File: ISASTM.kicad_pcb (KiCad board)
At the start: 2 copper layers, 1 part, among them J1 Bus_ISA_16bit

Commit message: Add connector
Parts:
- J1: value Bus_ISA_16bit -> Bus_ISA_8bit; footprint isastm:ISA16 -> ISASTM:Conn_Edge_PCB_ISA8
- moved J1 43.0 mm to (76.2, 112.4)
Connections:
- net Net-(J1-Pad11) renamed /~SMEMW
- net Net-(J1-Pad12) renamed /~SMEMR
- net Net-(J1-Pad13) renamed /~IOW
- net Net-(J1-Pad14) renamed /~IOR
- net Net-(J1-Pad15) renamed /~DACK3
- net Net-(J1-Pad16) renamed /DRQ3
- net Net-(J1-Pad17) renamed /~DACK1
- net Net-(J1-Pad18) renamed /DRQ1
- net Net-(J1-Pad19) renamed /~REFRESH
- net Net-(J1-Pad2) renamed /RESET
- net Net-(J1-Pad20) renamed /CLK
- net Net-(J1-Pad21) renamed /IRQ7
- net Net-(J1-Pad22) renamed /IRQ6
- net Net-(J1-Pad23) renamed /IRQ5
- net Net-(J1-Pad24) renamed /IRQ4
- net Net-(J1-Pad25) renamed /IRQ3
- net Net-(J1-Pad26) renamed /~DACK2
- net Net-(J1-Pad27) renamed /TC
- net Net-(J1-Pad28) renamed /ALE
- net Net-(J1-Pad30) renamed /OSC
- net Net-(J1-Pad32) renamed /~IO_CH_CK
- net Net-(J1-Pad33) renamed /D7
- net Net-(J1-Pad34) renamed /D6
- net Net-(J1-Pad35) renamed /D5
- net Net-(J1-Pad36) renamed /D4
- net Net-(J1-Pad37) renamed /D3
- net Net-(J1-Pad38) renamed /D2
- net Net-(J1-Pad39) renamed /D1
- net Net-(J1-Pad4) renamed /IRQ2
- net Net-(J1-Pad40) renamed /D0
- net Net-(J1-Pad41) renamed /IO_CH_RDY
- net Net-(J1-Pad42) renamed /AEN
- net Net-(J1-Pad43) renamed /A19
- net Net-(J1-Pad44) renamed /A18
- net Net-(J1-Pad45) renamed /A17
- net Net-(J1-Pad46) renamed /A16
- net Net-(J1-Pad47) renamed /A15
- net Net-(J1-Pad48) renamed /A14
- net Net-(J1-Pad49) renamed /A13
- net Net-(J1-Pad5) renamed -5V
- net Net-(J1-Pad50) renamed /A12
- net Net-(J1-Pad51) renamed /A11
- net Net-(J1-Pad52) renamed /A10
- net Net-(J1-Pad53) renamed /A9
- net Net-(J1-Pad54) renamed /A8
- net Net-(J1-Pad55) renamed /A7
- net Net-(J1-Pad56) renamed /A6
- net Net-(J1-Pad57) renamed /A5
- net Net-(J1-Pad58) renamed /A4
- net Net-(J1-Pad59) renamed /A3
- net Net-(J1-Pad6) renamed /DRQ2
- net Net-(J1-Pad60) renamed /A2
- net Net-(J1-Pad61) renamed /A1
- net Net-(J1-Pad62) renamed /A0
- net Net-(J1-Pad7) renamed -12V
- net Net-(J1-Pad9) renamed +12V
- J1 pad 29: Net-(J1-Pad29) -> +5V
- J1 pad 3: Net-(J1-Pad3) -> +5V
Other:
- board outline added: 101.6 x 101.6 mm
- copper layers 2 -> 4
- board text added: "Back ->"

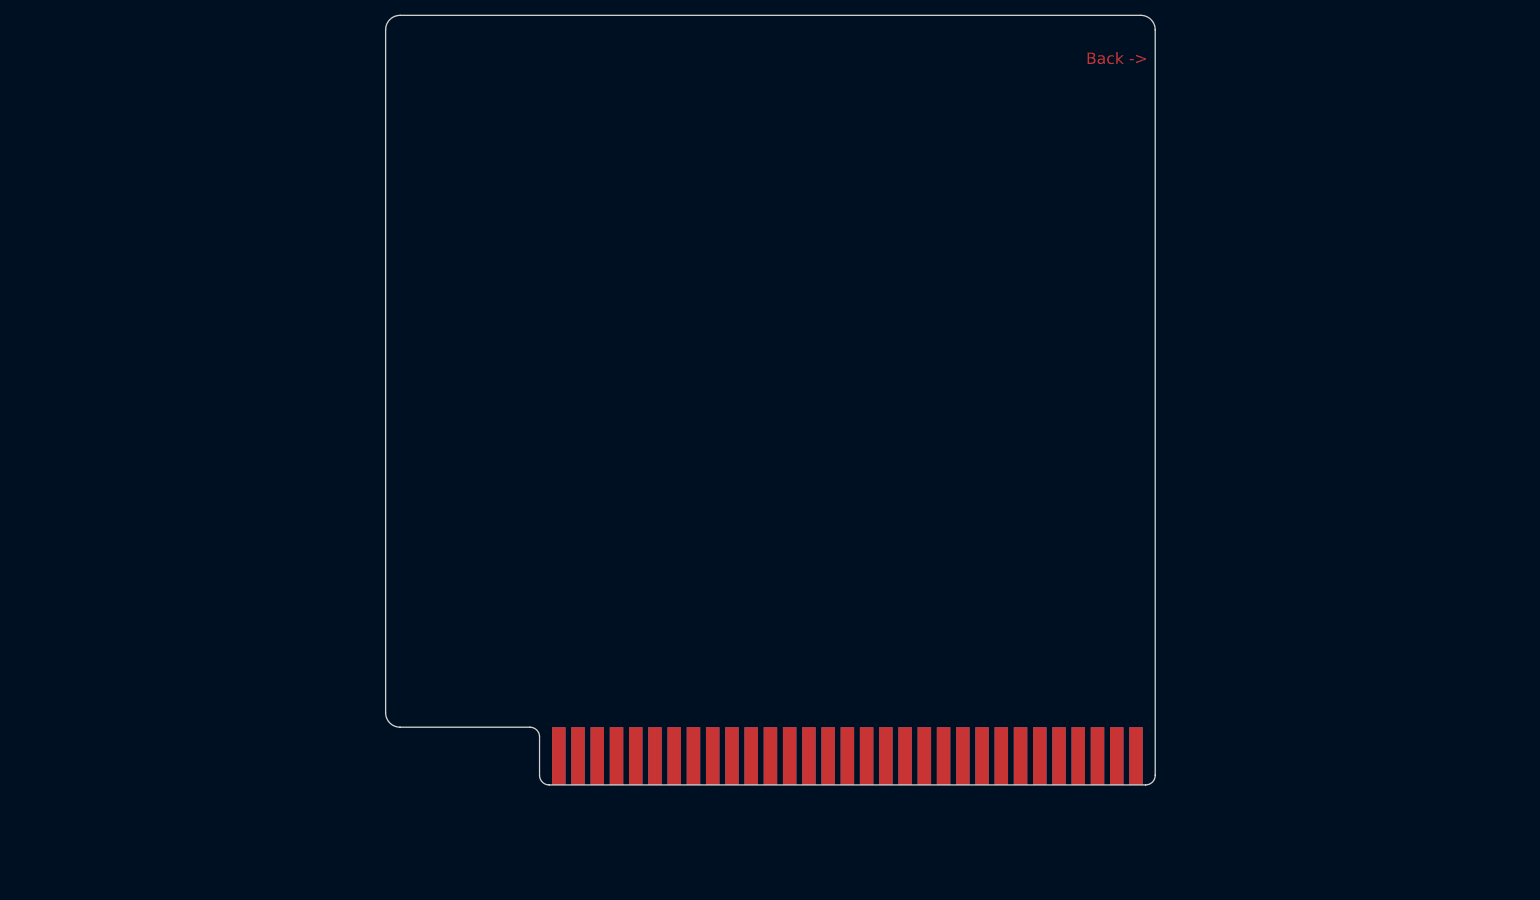
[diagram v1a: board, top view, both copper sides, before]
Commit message: Add ISA bus, level shifters, memory pinout
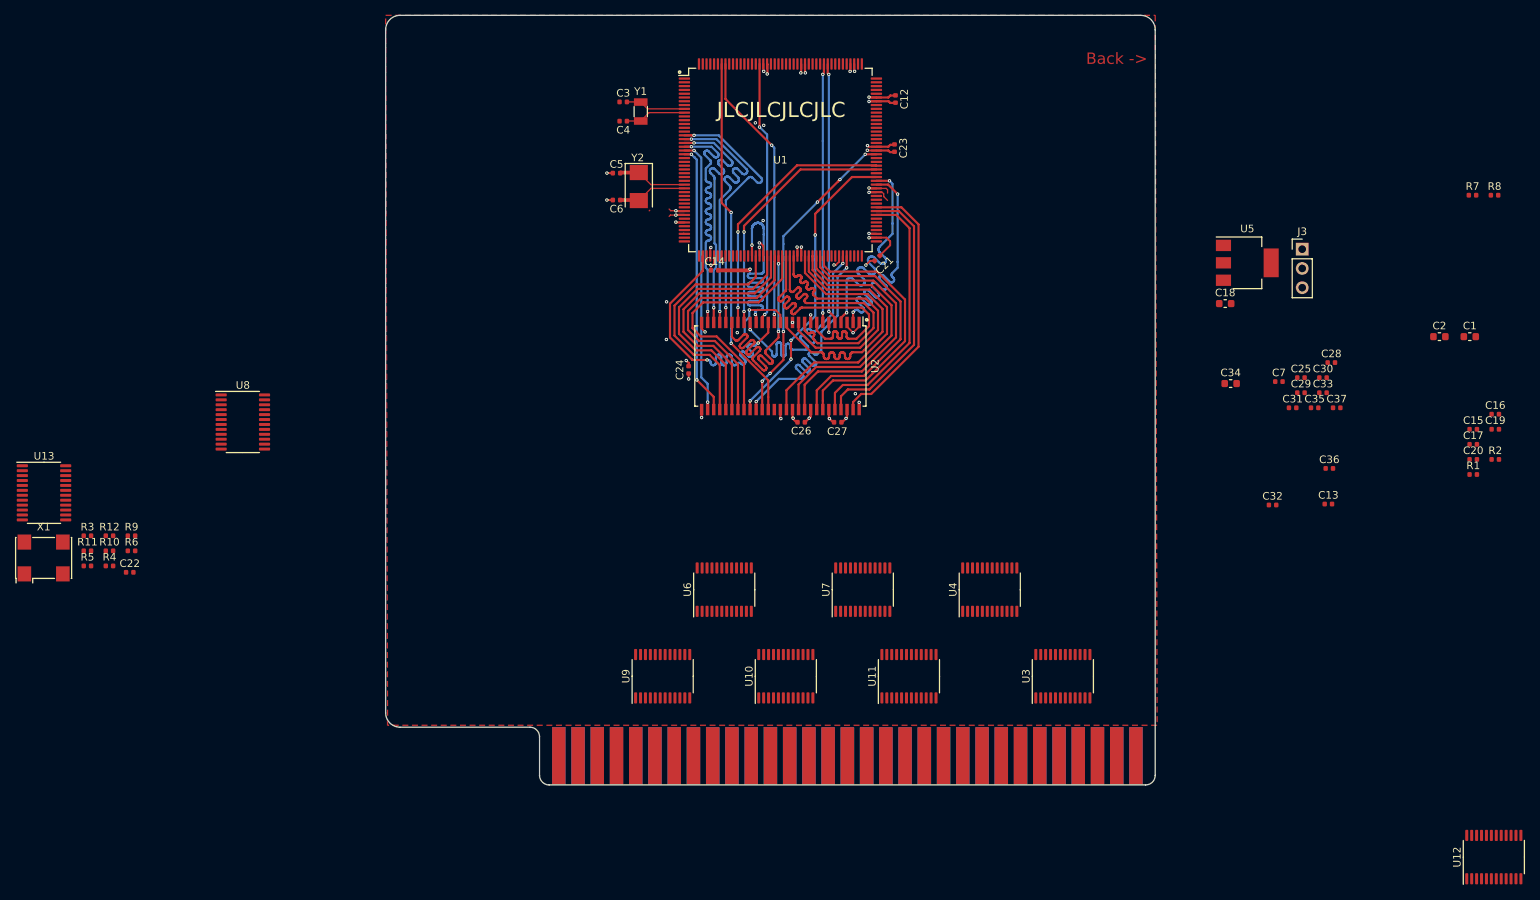
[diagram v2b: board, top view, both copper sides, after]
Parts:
- added C1: 2.2u, Capacitor_SMD:C_0603_1608Metric, F.Cu at (158.4, 57.0)
- added C12: 100n, Capacitor_SMD:C_0402_1005Metric, F.Cu at (82.5, 25.7)
- added C13: 100n, Capacitor_SMD:C_0402_1005Metric, F.Cu at (139.7, 79.1)
- added C14: 100n, Capacitor_SMD:C_0402_1005Metric, F.Cu at (58.7, 48.3)
- added C15: 100n, Capacitor_SMD:C_0402_1005Metric, F.Cu at (158.8, 69.3)
- added C16: 100n, Capacitor_SMD:C_0402_1005Metric, F.Cu at (161.7, 67.3)
- added C17: 100n, Capacitor_SMD:C_0402_1005Metric, F.Cu at (158.8, 71.2)
- added C18: 10u, Capacitor_SMD:C_0603_1608Metric, F.Cu at (126.1, 52.7)
- added C19: 100n, Capacitor_SMD:C_0402_1005Metric, F.Cu at (161.7, 69.3)
- added C2: 2.2u, Capacitor_SMD:C_0603_1608Metric, F.Cu at (154.4, 57.0)
- added C20: 100n, Capacitor_SMD:C_0402_1005Metric, F.Cu at (158.8, 73.2)
- added C21: 100n, Capacitor_SMD:C_0402_1005Metric, F.Cu at (80.1, 46.7)
- added C22: 100n, Capacitor_SMD:C_0402_1005Metric, F.Cu at (-18.5, 88.1)
- added C23: 100n, Capacitor_SMD:C_0402_1005Metric, F.Cu at (82.4, 32.1)
- added C24: 100n, Capacitor_SMD:C_0402_1005Metric, F.Cu at (55.2, 61.4)
- added C25: 100n, Capacitor_SMD:C_0402_1005Metric, F.Cu at (136.1, 62.4)
- added C26: 100n, Capacitor_SMD:C_0402_1005Metric, F.Cu at (70.1, 68.3)
- added C27: 100n, Capacitor_SMD:C_0402_1005Metric, F.Cu at (74.9, 68.3)
- added C28: 100n, Capacitor_SMD:C_0402_1005Metric, F.Cu at (140.1, 60.4)
- added C29: 100n, Capacitor_SMD:C_0402_1005Metric, F.Cu at (136.1, 64.4)
- added C3: 6p, Capacitor_SMD:C_0402_1005Metric, F.Cu at (46.6, 26.0)
- added C30: 100n, Capacitor_SMD:C_0402_1005Metric, F.Cu at (139.0, 62.4)
- added C31: 100n, Capacitor_SMD:C_0402_1005Metric, F.Cu at (135.0, 66.4)
- added C32: 100n, Capacitor_SMD:C_0402_1005Metric, F.Cu at (132.3, 79.2)
- added C33: 1u, Capacitor_SMD:C_0402_1005Metric, F.Cu at (139.0, 64.4)
- added C34: 22u, Capacitor_SMD:C_0603_1608Metric, F.Cu at (126.8, 63.2)
- added C35: 100n, Capacitor_SMD:C_0402_1005Metric, F.Cu at (137.9, 66.4)
- added C36: 100n, Capacitor_SMD:C_0402_1005Metric, F.Cu at (139.8, 74.4)
- added C37: 100n, Capacitor_SMD:C_0402_1005Metric, F.Cu at (140.8, 66.4)
- added C4: 6p, Capacitor_SMD:C_0402_1005Metric, F.Cu at (46.6, 28.6)
- added C5: 20p, Capacitor_SMD:C_0402_1005Metric, F.Cu at (45.7, 35.4)
- added C6: 20p, Capacitor_SMD:C_0402_1005Metric, F.Cu at (45.7, 39.0)
- added C7: 1u, Capacitor_SMD:C_0402_1005Metric, F.Cu at (133.2, 63.0)
- added J3: Boot select, Connector_PinHeader_2.54mm:PinHeader_1x03_P2.54mm_Vertical, F.Cu at (136.2, 45.5)
- added R1: 10k, Resistor_SMD:R_0402_1005Metric, F.Cu at (158.8, 75.2)
- added R10: 10k, Resistor_SMD:R_0402_1005Metric, F.Cu at (-21.2, 85.3)
- added R11: 10k, Resistor_SMD:R_0402_1005Metric, F.Cu at (-24.1, 85.3)
- added R12: 10k, Resistor_SMD:R_0402_1005Metric, F.Cu at (-21.2, 83.3)
- added R2: 10R, Resistor_SMD:R_0402_1005Metric, F.Cu at (161.7, 73.2)
- added R3: 10k, Resistor_SMD:R_0402_1005Metric, F.Cu at (-24.1, 83.3)
- added R4: 10k, Resistor_SMD:R_0402_1005Metric, F.Cu at (-21.2, 87.3)
- added R5: 10k, Resistor_SMD:R_0402_1005Metric, F.Cu at (-24.1, 87.3)
- added R6: 10k, Resistor_SMD:R_0402_1005Metric, F.Cu at (-18.3, 85.3)
- added R7: 10k, Resistor_SMD:R_0402_1005Metric, F.Cu at (158.7, 38.4)
- added R8: 100k, Resistor_SMD:R_0402_1005Metric, F.Cu at (161.6, 38.4)
- added R9: 10k, Resistor_SMD:R_0402_1005Metric, F.Cu at (-18.3, 83.3)
- added U1: STM32H743IITx, Package_QFP:LQFP-176_24x24mm_P0.5mm, F.Cu at (67.4, 33.7)
- added U10: SN74AVC8T245PW, Package_SO:TSSOP-24_4.4x7.8mm_P0.65mm, F.Cu at (68.1, 101.9)
- added U11: SN74AVC8T245PW, Package_SO:TSSOP-24_4.4x7.8mm_P0.65mm, F.Cu at (84.3, 101.9)
- added U12: SN74AVC8T245PW, Package_SO:TSSOP-24_4.4x7.8mm_P0.65mm, F.Cu at (161.5, 125.7)
- added U13: SN74AVC8T245PW, Package_SO:TSSOP-24_4.4x7.8mm_P0.65mm, F.Cu at (-29.9, 77.6)
- added U2: MT48LC16M16A2P, Package_SO:TSOP-II-54_22.2x10.16mm_P0.8mm, F.Cu at (67.4, 60.9)
- added U3: SN74AVC8T245PW, Package_SO:TSSOP-24_4.4x7.8mm_P0.65mm, F.Cu at (104.6, 101.9)
- added U4: SN74AVC8T245PW, Package_SO:TSSOP-24_4.4x7.8mm_P0.65mm, F.Cu at (95.0, 90.4)
- added U5: AMS1117-3.3, Package_TO_SOT_SMD:SOT-223-3_TabPin2, F.Cu at (129.0, 47.3)
- added U6: SN74AVC8T245PW, Package_SO:TSSOP-24_4.4x7.8mm_P0.65mm, F.Cu at (59.9, 90.4)
- added U7: SN74AVC8T245PW, Package_SO:TSSOP-24_4.4x7.8mm_P0.65mm, F.Cu at (78.2, 90.4)
- added U8: SN74AVC8T245PW, Package_SO:TSSOP-24_4.4x7.8mm_P0.65mm, F.Cu at (-3.61, 68.3)
- added U9: SN74AVC8T245PW, Package_SO:TSSOP-24_4.4x7.8mm_P0.65mm, F.Cu at (51.8, 101.9)
- added X1: SG-7050CAN, Oscillator:Oscillator_SMD_SeikoEpson_SG8002CA-4Pin_7.0x5.0mm, F.Cu at (-29.9, 86.2)
- added Y1: 32.768 kHz, Crystal:Crystal_SMD_3215-2Pin_3.2x1.5mm, F.Cu at (48.9, 27.3)
- added Y2: 8 MHz, Crystal:Crystal_SMD_5032-2Pin_5.0x3.2mm, F.Cu at (48.7, 37.2)
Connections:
- J1 pad 2: /RESET -> /ISARESET
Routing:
- net /MEM_PE1: track 0.00 -> 48.3 mm, vias 0 -> 2
- net +3V3: track 0.00 -> 45.2 mm, vias 0 -> 21
- net /MEM_PG8: track 0.00 -> 40.8 mm, vias 0 -> 6
- net GND: track 0.00 -> 40.6 mm, vias 0 -> 24
- net /MEM_PG2: track 0.00 -> 39.7 mm, vias 0 -> 4
- net /MEM_PH5: track 0.00 -> 39.5 mm, vias 0 -> 2
- net /MEM_PE7: track 0.00 -> 37.5 mm
- net /MEM_PG0: track 0.00 -> 37.3 mm, vias 0 -> 2
- net /MEM_PE10: track 0.00 -> 36.9 mm
- net /MEM_PE0: track 0.00 -> 36.8 mm, vias 0 -> 2
- net /MEM_PE11: track 0.00 -> 36.8 mm
- net /MEM_PE12: track 0.00 -> 36.5 mm
- net /MEM_PE13: track 0.00 -> 36.5 mm
- net /MEM_PF1: track 0.00 -> 36.4 mm, vias 0 -> 2
- net /MEM_PF4: track 0.00 -> 36.2 mm, vias 0 -> 2
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- added copper zone on In2.Cu, net +3V3
- added copper zone on F.Cu, net GND
- added copper zone on In1.Cu, net GND
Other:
- net class Default: clearance 0.2 -> 0.127; trace_width 0.25 -> 0.127; via_dia 0.8 -> 0.45; via_drill 0.4 -> 0.2
- rule trace_clearance: 0.2 -> 0.127
- rule trace_min: 0.2 -> 0.127
- rule via_min_drill: 0.3 -> 0.2
- rule via_min_size: 0.4 -> 0.45
- board text added: "JLCJLCJLCJLC"

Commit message: Add more decoupling
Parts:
- added C10: 1u, Capacitor_SMD:C_0402_1005Metric, F.Cu at (-16.0, 33.1)
- added C11: 1u, Capacitor_SMD:C_0402_1005Metric, F.Cu at (-5.62, 22.2)
- added C38: 100n, Capacitor_SMD:C_0402_1005Metric, F.Cu at (-36.9, 42.1)
- added C39: 100n, Capacitor_SMD:C_0402_1005Metric, F.Cu at (-34.0, 42.1)
- added C40: 100n, Capacitor_SMD:C_0402_1005Metric, F.Cu at (134.6, 120.0)
- added C41: 100n, Capacitor_SMD:C_0402_1005Metric, F.Cu at (134.6, 122.0)
- added C42: 100n, Capacitor_SMD:C_0402_1005Metric, F.Cu at (137.5, 120.0)
- added C43: 100n, Capacitor_SMD:C_0402_1005Metric, F.Cu at (134.6, 124.0)
- added C44: 100n, Capacitor_SMD:C_0402_1005Metric, F.Cu at (137.5, 122.0)
- added C45: 100n, Capacitor_SMD:C_0402_1005Metric, F.Cu at (140.4, 120.0)
- added C46: 100n, Capacitor_SMD:C_0402_1005Metric, F.Cu at (134.6, 126.0)
- added C47: 100n, Capacitor_SMD:C_0402_1005Metric, F.Cu at (137.5, 124.0)
- added C48: 100n, Capacitor_SMD:C_0402_1005Metric, F.Cu at (140.4, 122.0)
- added C49: 100n, Capacitor_SMD:C_0402_1005Metric, F.Cu at (143.3, 120.0)
- added C50: 100n, Capacitor_SMD:C_0402_1005Metric, F.Cu at (137.5, 126.0)
- added C51: 100n, Capacitor_SMD:C_0402_1005Metric, F.Cu at (140.4, 124.0)
- added C52: 100n, Capacitor_SMD:C_0402_1005Metric, F.Cu at (143.3, 122.0)
- added C53: 100n, Capacitor_SMD:C_0402_1005Metric, F.Cu at (146.3, 120.0)
- added C54: 100n, Capacitor_SMD:C_0402_1005Metric, F.Cu at (140.4, 126.0)
- added C55: 100n, Capacitor_SMD:C_0402_1005Metric, F.Cu at (143.3, 124.0)
- added C56: 100n, Capacitor_SMD:C_0402_1005Metric, F.Cu at (146.3, 122.0)
- added C57: 100n, Capacitor_SMD:C_0402_1005Metric, F.Cu at (143.3, 126.0)
- added C58: 100n, Capacitor_SMD:C_0402_1005Metric, F.Cu at (146.3, 124.0)
- added C59: 100n, Capacitor_SMD:C_0402_1005Metric, F.Cu at (146.3, 126.0)
- added C8: 6.8pF, Capacitor_SMD:C_0402_1005Metric, F.Cu at (-15.4, 41.0)
- added C9: 100n, Capacitor_SMD:C_0402_1005Metric, F.Cu at (-31.1, 42.1)
- added D1: White, LED_SMD:LED_0603_1608Metric, F.Cu at (-11.8, 28.7)
- added D2: Red, LED_SMD:LED_0603_1608Metric, F.Cu at (-24.7, 38.1)
- added D3: Yellow, LED_SMD:LED_0603_1608Metric, F.Cu at (-19.5, 33.6)
- added D4: Green, LED_SMD:LED_0603_1608Metric, F.Cu at (-24.7, 40.7)
- added D5: Blue, LED_SMD:LED_0603_1608Metric, F.Cu at (-9.38, 26.0)
- added J2: USB_C_Receptacle_USB2.0, Connector_USB:USB_C_Receptacle_Palconn_UTC16-G, F.Cu at (112.5, 41.7)
- added J4: USB_C_Receptacle_USB2.0, Connector_USB:USB_C_Receptacle_Palconn_UTC16-G, F.Cu at (112.5, 23.5)
- added J5: TagConnect_TC2030_SWD, Connector:Tag-Connect_TC2030-IDC-NL_2x03_P1.27mm_Vertical, F.Cu at (91.4, 17.9)
- added JP1: SolderJumper_2_Open, Jumper:SolderJumper-2_P1.3mm_Open_Pad1.0x1.5mm, F.Cu at (-30.5, 15.9)
- added R13: 5.1k, Resistor_SMD:R_0402_1005Metric, F.Cu at (-5.62, 24.2)
- added R14: 5.1k, Resistor_SMD:R_0402_1005Metric, F.Cu at (-12.4, 31.0)
- added R15: 5.1k, Resistor_SMD:R_0402_1005Metric, F.Cu at (-21.3, 40.4)
- added R16: 5.1k, Resistor_SMD:R_0402_1005Metric, F.Cu at (-2.71, 22.2)
- added R17: 1M, Resistor_SMD:R_0402_1005Metric, F.Cu at (-8.35, 28.3)
- added R18: 20k, Resistor_SMD:R_0402_1005Metric, F.Cu at (-13.1, 33.1)
- added R19: 7.5k, Resistor_SMD:R_0402_1005Metric, F.Cu at (-18.3, 38.4)
- added R20: 560R, Resistor_SMD:R_0603_1608Metric, F.Cu at (-19.5, 36.2)
- added R21: 5.1k, Resistor_SMD:R_0402_1005Metric, F.Cu at (-5.92, 26.1)
- added R22: 5.1k, Resistor_SMD:R_0402_1005Metric, F.Cu at (-13.1, 35.1)
- added R23: 5.1k, Resistor_SMD:R_0402_1005Metric, F.Cu at (-21.3, 38.4)
- added R24: 5.1k, Resistor_SMD:R_0402_1005Metric, F.Cu at (-0.10, 26.1)
- added R25: 5.1k, Resistor_SMD:R_0402_1005Metric, F.Cu at (-21.3, 42.4)
- added R26: 100k, Resistor_SMD:R_0402_1005Metric, F.Cu at (-18.3, 40.4)
- added R27: 100k, Resistor_SMD:R_0402_1005Metric, F.Cu at (-5.44, 28.1)
- added R28: 100k, Resistor_SMD:R_0402_1005Metric, F.Cu at (-10.2, 33.0)
- added R29: 100k, Resistor_SMD:R_0402_1005Metric, F.Cu at (-15.4, 37.0)
- added R30: 100k, Resistor_SMD:R_0402_1005Metric, F.Cu at (-3.01, 26.1)
- added R31: 100k, Resistor_SMD:R_0402_1005Metric, F.Cu at (-15.4, 39.0)
- added R32: 100k, Resistor_SMD:R_0402_1005Metric, F.Cu at (-10.2, 35.0)
- added R33: 100k, Resistor_SMD:R_0402_1005Metric, F.Cu at (-12.5, 37.0)
- added R34: 100k, Resistor_SMD:R_0402_1005Metric, F.Cu at (-5.44, 30.1)
- added R35: 1k, Resistor_SMD:R_0402_1005Metric, F.Cu at (-18.3, 42.4)
- added R36: 4.7k, Resistor_SMD:R_0402_1005Metric, F.Cu at (-2.53, 28.1)
- added R37: 4.7k, Resistor_SMD:R_0402_1005Metric, F.Cu at (-2.71, 24.2)
- added R38: 4.7k, Resistor_SMD:R_0402_1005Metric, F.Cu at (-7.27, 32.3)
- added R39: 4.7k, Resistor_SMD:R_0402_1005Metric, F.Cu at (-8.35, 30.3)
- added R40: 4.7k, Resistor_SMD:R_0402_1005Metric, F.Cu at (-12.5, 39.0)
- added R41: 100k, Resistor_SMD:R_0402_1005Metric, F.Cu at (-7.27, 34.3)
- added R42: 100k, Resistor_SMD:R_0402_1005Metric, F.Cu at (-2.53, 30.1)
- added R43: 100k, Resistor_SMD:R_0402_1005Metric, F.Cu at (-9.61, 37.0)
- added R44: 100k, Resistor_SMD:R_0402_1005Metric, F.Cu at (-12.5, 41.0)
- added R45: 100k, Resistor_SMD:R_0402_1005Metric, F.Cu at (-4.36, 32.1)
- added R46: 100k, Resistor_SMD:R_0402_1005Metric, F.Cu at (-9.61, 39.0)
- added R47: 100k, Resistor_SMD:R_0402_1005Metric, F.Cu at (-4.36, 34.1)
- added R48: 100k, Resistor_SMD:R_0402_1005Metric, F.Cu at (-6.70, 36.3)
- added SW1: Reset, ISASTM:TS-1187A-X-X-X, F.Cu at (102.1, 17.8)
- added U14: SRV05-4, Package_TO_SOT_SMD:SOT-23-6, F.Cu at (102.7, 23.7)
- added U15: USB3343, Package_DFN_QFN:QFN-24-1EP_4x4mm_P0.5mm_EP2.6x2.6mm, F.Cu at (-70.4, 47.8)
- C3: value 6p -> 6.8pF
- C4: value 6p -> 1u
- Y1: value 32.768 kHz -> 26 MHz; footprint Crystal:Crystal_SMD_3215-2Pin_3.2x1.5mm -> Crystal:Crystal_SMD_3225-4Pin_3.2x2.5mm
- moved X1 183.6 mm to (153.7, 89.5)
- moved U12 141.7 mm to (30.5, 71.8)
- moved Y1 123.5 mm to (-71.8, 53.7), turned to 0 degrees
- moved U5 119.5 mm to (22.0, 100.5), turned to 90 degrees
- moved U8 116.1 mm to (111.0, 87.0), turned to 90 degrees
- moved C28 90.0 mm to (52.3, 40.6), turned to 270 degrees
- moved R7 78.3 mm to (82.5, 20.2), turned to 270 degrees
- moved C37 65.1 mm to (81.8, 38.9), turned to 270 degrees
- moved C3 63.3 mm to (-16.0, 35.1)
- moved J3 63.0 mm to (80.0, 17.1), turned to 90 degrees
- moved U13 61.1 mm to (30.5, 87.0), turned to 90 degrees
- moved C4 57.6 mm to (-9.61, 41.0), turned to 0 degrees
- moved R8 57.3 mm to (108.0, 18.4), turned to 270 degrees
- moved U9 13.3 mm to (40.6, 94.6)
- moved U10 10.1 mm to (61.0, 94.6)
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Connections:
- net /ADDRESS_OE renamed /~ADDRESS_OE
- net /RESET renamed /~RESET
- C3 pad 1: GND -> Net-(C3-Pad1)
- C3 pad 2: /PC14 -> GND
- C4 pad 1: /PC15 -> Net-(C4-Pad1)
- J1 pad 8: Net-(J1-Pad8) -> /~NOWS
- U1 pad 10: Net-(U1-Pad10) -> /LV_A15
- U1 pad 11: Net-(U1-Pad11) -> /LV_A17
- U1 pad 115: Net-(U1-Pad115) -> /~LV_NOWS
- U1 pad 117: Net-(U1-Pad117) -> /LV_A8
- U1 pad 118: Net-(U1-Pad118) -> /LV_A9
- U1 pad 119: Net-(U1-Pad119) -> /~LV_DACK3
- U1 pad 12: Net-(U1-Pad12) -> /LV_A18
- U1 pad 120: Net-(U1-Pad120) -> /LV_AEN
- U1 pad 121: Net-(U1-Pad121) -> /LV_ALE
- U1 pad 122: /USB_HOST_D- -> /USB_FS_D-
- U1 pad 123: /USB_HOST_D+ -> /USB_FS_D+
- U1 pad 124: Net-(U1-Pad124) -> /SWDIO
- U1 pad 128: Net-(U1-Pad128) -> /LV_A5
- U1 pad 129: Net-(U1-Pad129) -> /LV_A6
- U1 pad 13: Net-(U1-Pad13) -> /LV_A19
- U1 pad 130: Net-(U1-Pad130) -> /LV_A7
- U1 pad 131: Net-(U1-Pad131) -> /LV_D0
- U1 pad 132: Net-(U1-Pad132) -> /LV_D1
- U1 pad 133: Net-(U1-Pad133) -> /LV_D2
- U1 pad 134: Net-(U1-Pad134) -> /LV_D3
- U1 pad 137: Net-(U1-Pad137) -> /SWCLK
- U1 pad 139: Net-(U1-Pad139) -> /LV_A10
- U1 pad 140: Net-(U1-Pad140) -> /LV_A11
- U1 pad 141: Net-(U1-Pad141) -> /LV_A12
- U1 pad 144: Net-(U1-Pad144) -> /LV_IRQ2
- U1 pad 145: Net-(U1-Pad145) -> /LV_IRQ3
- U1 pad 146: Net-(U1-Pad146) -> /LV_IRQ4
- U1 pad 147: Net-(U1-Pad147) -> /LV_IRQ5
- U1 pad 150: Net-(U1-Pad150) -> /LV_IRQ6
- U1 pad 151: Net-(U1-Pad151) -> /LV_IRQ7
- U1 pad 152: Net-(U1-Pad152) -> /LED1
- U1 pad 153: Net-(U1-Pad153) -> /LED2
- U1 pad 154: Net-(U1-Pad154) -> /LED3
- U1 pad 155: Net-(U1-Pad155) -> /LED4
- U1 pad 156: Net-(U1-Pad156) -> /LED5
- U1 pad 161: Net-(U1-Pad161) -> /SWO
- U1 pad 162: Net-(U1-Pad162) -> /~REFRESH
- U1 pad 163: Net-(U1-Pad163) -> /OTG_HS_ULPI_D7
- U1 pad 164: Net-(U1-Pad164) -> /~LV_SMEMW
- U1 pad 165: Net-(U1-Pad165) -> /~LV_SMEMR
- U1 pad 167: Net-(U1-Pad167) -> /~LV_IOW
- U1 pad 168: Net-(U1-Pad168) -> /~LV_IOR
- U1 pad 173: Net-(U1-Pad173) -> /LV_D4
- U1 pad 174: Net-(U1-Pad174) -> /LV_D5
- U1 pad 175: Net-(U1-Pad175) -> /LV_D6
- U1 pad 176: Net-(U1-Pad176) -> /LV_D7
- U1 pad 32: Net-(U1-Pad32) -> /OTG_HS_ULPI_STP
- U1 pad 34: Net-(U1-Pad34) -> /OTG_HS_ULPI_DIR
- U1 pad 35: Net-(U1-Pad35) -> /OTG_HS_ULPI_NXT
- U1 pad 40: Net-(U1-Pad40) -> /LV_DRQ1
- U1 pad 41: Net-(U1-Pad41) -> /LV_DRQ2
- U1 pad 42: Net-(U1-Pad42) -> /LV_DRQ3
- U1 pad 47: Net-(U1-Pad47) -> /OTG_HS_ULPI_D0
- U1 pad 50: Net-(U1-Pad50) -> /LV_ISARESET
- U1 pad 51: Net-(U1-Pad51) -> /OTG_HS_ULPI_CK
- U1 pad 52: Net-(U1-Pad52) -> /~LV_DACK1
- U1 pad 53: Net-(U1-Pad53) -> /~LV_DACK2
- U1 pad 54: Net-(U1-Pad54) -> /LV_TC
- U1 pad 55: Net-(U1-Pad55) -> /LV_CLK
- U1 pad 56: Net-(U1-Pad56) -> /OTG_HS_ULPI_D1
- U1 pad 57: Net-(U1-Pad57) -> /OTG_HS_ULPI_D2
- U1 pad 58: Net-(U1-Pad58) -> /LV_IO_CH_RDY
- U1 pad 7: Net-(U1-Pad7) -> /LV_A16
- U1 pad 79: Net-(U1-Pad79) -> /OTG_HS_ULPI_D3
- U1 pad 8: Net-(U1-Pad8) -> /LV_A13
- U1 pad 80: Net-(U1-Pad80) -> /OTG_HS_ULPI_D4
- U1 pad 85: Net-(U1-Pad85) -> /LV_A0
- U1 pad 86: Net-(U1-Pad86) -> /LV_A1
- U1 pad 87: Net-(U1-Pad87) -> /LV_A2
- U1 pad 88: Net-(U1-Pad88) -> /LV_A3
- U1 pad 89: Net-(U1-Pad89) -> /LV_A4
- U1 pad 9: Net-(U1-Pad9) -> /LV_A14
- U1 pad 92: Net-(U1-Pad92) -> /OTG_HS_ULPI_D5
- U1 pad 93: Net-(U1-Pad93) -> /OTG_HS_ULPI_D6
- U1 pad 94: Net-(U1-Pad94) -> /~LV_IO_CH_CK
- U10 pad 14: Net-(U10-Pad14) -> /LV_A15
- U10 pad 15: Net-(U10-Pad15) -> /LV_A14
- U10 pad 16: Net-(U10-Pad16) -> /LV_A13
- U10 pad 17: Net-(U10-Pad17) -> /LV_A12
- U10 pad 18: Net-(U10-Pad18) -> /LV_A11
- U10 pad 19: Net-(U10-Pad19) -> /LV_A10
- U10 pad 20: Net-(U10-Pad20) -> /LV_A9
- U10 pad 21: Net-(U10-Pad21) -> /LV_A8
- U11 pad 10: /OSC -> GND
- U11 pad 14: Net-(U11-Pad14) -> GND
- U11 pad 15: Net-(U11-Pad15) -> GND
- U11 pad 16: Net-(U11-Pad16) -> GND
- U11 pad 17: Net-(U11-Pad17) -> GND
- U11 pad 18: Net-(U11-Pad18) -> /LV_A19
- U11 pad 19: Net-(U11-Pad19) -> /LV_A18
- U11 pad 20: Net-(U11-Pad20) -> /LV_A17
- U11 pad 21: Net-(U11-Pad21) -> /LV_A16
- U11 pad 7: Net-(U11-Pad7) -> GND
- U11 pad 8: Net-(U11-Pad8) -> GND
- U11 pad 9: Net-(U11-Pad9) -> GND
- U12 pad 10: Net-(U12-Pad10) -> GND
- U12 pad 14: Net-(U12-Pad14) -> GND
- U12 pad 16: Net-(U12-Pad16) -> /~LV_NOWS
- U12 pad 17: Net-(U12-Pad17) -> /LV_CLK
- U12 pad 18: Net-(U12-Pad18) -> /LV_TC
- U12 pad 19: Net-(U12-Pad19) -> /~LV_DACK3
- U12 pad 20: Net-(U12-Pad20) -> /~LV_DACK2
- U12 pad 21: Net-(U12-Pad21) -> /~LV_DACK1
- U12 pad 22: /CONTROL3_OE -> /~CONTROL3_OE
- U12 pad 6: Net-(U12-Pad6) -> /TC
- U12 pad 7: Net-(U12-Pad7) -> /CLK
- U12 pad 8: Net-(U12-Pad8) -> /~NOWS
- U12 pad 9: Net-(U12-Pad9) -> /OSC
- U13 pad 22: /SPARE2_OE -> /~SPARE2_OE
- U3 pad 14: Net-(U3-Pad14) -> /LV_D7
- U3 pad 15: Net-(U3-Pad15) -> /LV_D6
- U3 pad 16: Net-(U3-Pad16) -> /LV_D5
- U3 pad 17: Net-(U3-Pad17) -> /LV_D4
- U3 pad 18: Net-(U3-Pad18) -> /LV_D3
- U3 pad 19: Net-(U3-Pad19) -> /LV_D2
- U3 pad 20: Net-(U3-Pad20) -> /LV_D1
- U3 pad 21: Net-(U3-Pad21) -> /LV_D0
- U3 pad 22: /DATA_OE -> /~DATA_OE
- U4 pad 10: /ISARESET -> GND
- U4 pad 14: Net-(U4-Pad14) -> GND
- U4 pad 15: Net-(U4-Pad15) -> /LV_ISARESET
- U4 pad 16: Net-(U4-Pad16) -> /LV_ALE
- U4 pad 17: Net-(U4-Pad17) -> /LV_AEN
- U4 pad 18: Net-(U4-Pad18) -> /~LV_SMEMW
- U4 pad 19: Net-(U4-Pad19) -> /~LV_SMEMR
- U4 pad 20: Net-(U4-Pad20) -> /~LV_IOW
- U4 pad 21: Net-(U4-Pad21) -> /~LV_IOR
- U4 pad 22: /CONTROL1_OE -> /~CONTROL1_OE
- U4 pad 3: /~SMEMW -> /~IOR
- U4 pad 4: /~SMEMR -> /~IOW
- U4 pad 5: /~IOW -> /~SMEMR
- U4 pad 6: /~IOR -> /~SMEMW
- U4 pad 9: /~REFRESH -> /ISARESET
- U6 pad 14: Net-(U6-Pad14) -> /~LV_IO_CH_CK
- U6 pad 15: Net-(U6-Pad15) -> /LV_IRQ7
- U6 pad 16: Net-(U6-Pad16) -> /LV_IRQ6
- U6 pad 17: Net-(U6-Pad17) -> /LV_IRQ5
- U6 pad 18: Net-(U6-Pad18) -> /LV_IRQ4
- U6 pad 19: Net-(U6-Pad19) -> /LV_IRQ3
- U6 pad 20: Net-(U6-Pad20) -> /LV_IRQ2
- U6 pad 21: Net-(U6-Pad21) -> /LV_IO_CH_RDY
- U6 pad 22: /IRQ_OE -> /~IRQ_OE
- U7 pad 10: Net-(U7-Pad10) -> GND
- U7 pad 14: Net-(U7-Pad14) -> GND
- U7 pad 15: Net-(U7-Pad15) -> GND
- U7 pad 16: Net-(U7-Pad16) -> GND
- U7 pad 17: Net-(U7-Pad17) -> GND
- U7 pad 18: Net-(U7-Pad18) -> GND
- U7 pad 19: Net-(U7-Pad19) -> /LV_DRQ3
- U7 pad 20: Net-(U7-Pad20) -> /LV_DRQ2
- U7 pad 21: Net-(U7-Pad21) -> /LV_DRQ1
- U7 pad 22: /CONTROL2_OE -> /~CONTROL2_OE
- U7 pad 6: Net-(U7-Pad6) -> GND
- U7 pad 7: Net-(U7-Pad7) -> GND
- U7 pad 8: Net-(U7-Pad8) -> GND
- U7 pad 9: Net-(U7-Pad9) -> GND
- U8 pad 22: /SPARE1_OE -> /~SPARE1_OE
- U9 pad 14: Net-(U9-Pad14) -> /LV_A7
- U9 pad 15: Net-(U9-Pad15) -> /LV_A6
- U9 pad 16: Net-(U9-Pad16) -> /LV_A5
- U9 pad 17: Net-(U9-Pad17) -> /LV_A4
- U9 pad 18: Net-(U9-Pad18) -> /LV_A3
- U9 pad 19: Net-(U9-Pad19) -> /LV_A2
- U9 pad 20: Net-(U9-Pad20) -> /LV_A1
- U9 pad 21: Net-(U9-Pad21) -> /LV_A0
- X1 pad 3: Net-(U11-Pad14) -> Net-(U12-Pad15)
- Y1 pad 1: /PC14 -> Net-(C3-Pad1)
- Y1 pad 2: /PC15 -> GND
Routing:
- net /PC15: track 8.03 -> 0.00 mm
- net /PC14: track 7.94 -> 0.00 mm
